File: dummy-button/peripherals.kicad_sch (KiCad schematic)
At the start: 45 parts, among them J2 repro_motor, Q1 MMBT2222A, Q2 MMBT2222A, SW1 RotaryEncoder_Switch_MP, T4 TestPoint, U1 MAX98357A, U5 DRV2605LDGS, U7 CD4051B

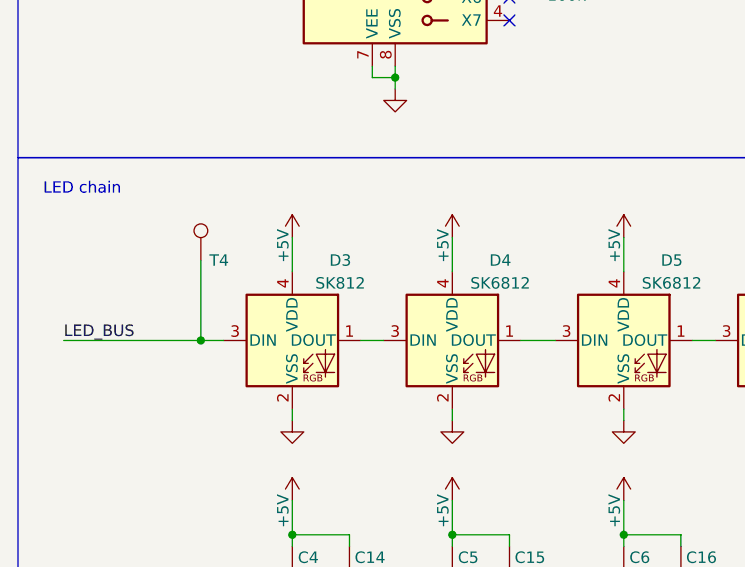
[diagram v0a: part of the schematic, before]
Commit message: rusty-boards: dummy-button: Fix SK6812 component value typo
- correct SK812 to SK6812 in peripherals schematic
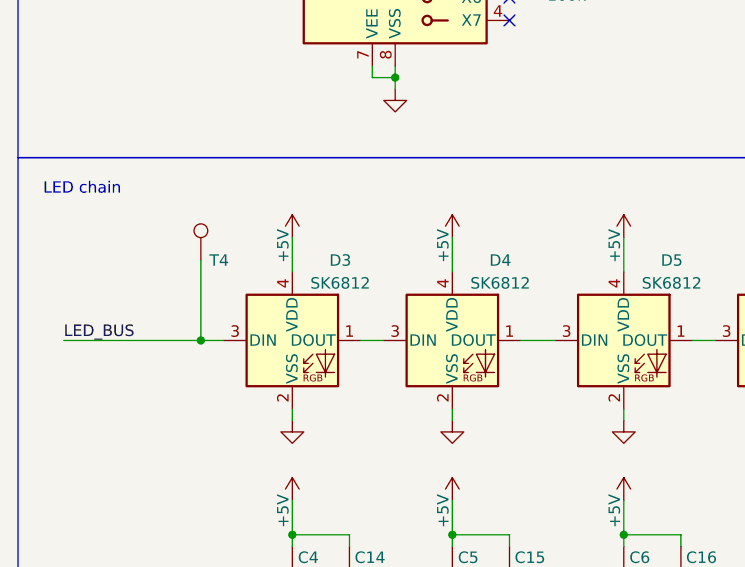
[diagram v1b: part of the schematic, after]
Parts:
- D3: value SK812 -> SK6812
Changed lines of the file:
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@@
 			)
 		)
-		(property "Value" "SK812"
+		(property "Value" "SK6812"
 			(at 56.134 143.51 0)
 			(effects
